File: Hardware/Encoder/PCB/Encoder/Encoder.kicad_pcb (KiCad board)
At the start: 2 copper layers, 17.8 x 29.8 mm, 2 parts, among them J1 Conn_01x06_Male, SW1 RotaryEncoder_Switch

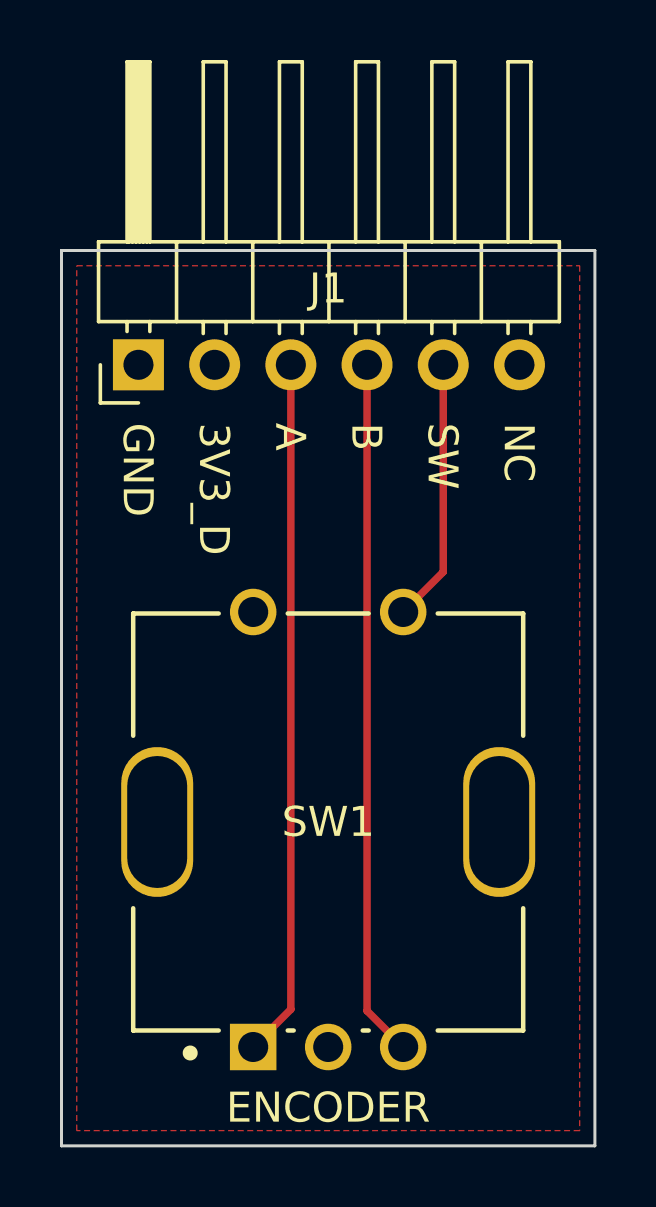
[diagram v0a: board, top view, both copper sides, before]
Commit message: menu screen added
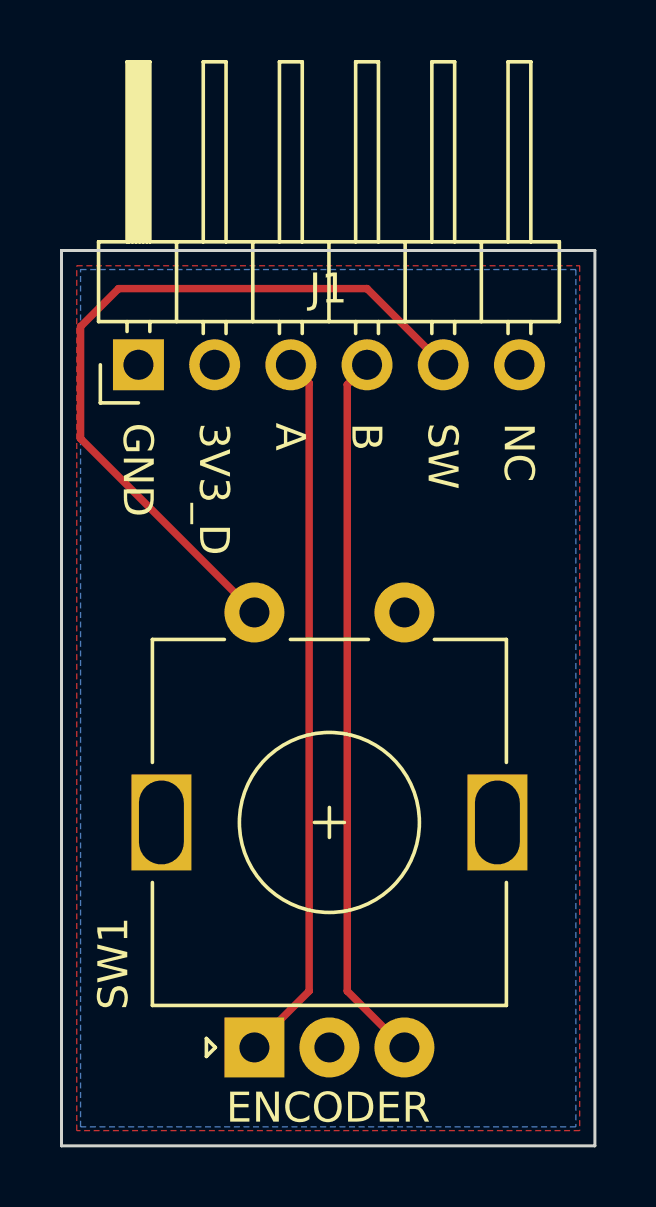
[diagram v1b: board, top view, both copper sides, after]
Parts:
- SW1: footprint RotaryEncoder:Bourns-PEC11R-4220F-S0024-0-0-0 -> Rotary_Encoder:RotaryEncoder_Alps_EC11E-Switch_Vertical_H20mm
- moved SW1 7.91 mm to (96.6, 86.3), turned to 90 degrees
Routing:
- net ENC_SW: track 8.79 -> 25.6 mm
- net ENC_B: track 23.2 -> 23.8 mm
- net ENC_A: track 23.3 -> 23.8 mm
- added copper zone on B.Cu, net GND
